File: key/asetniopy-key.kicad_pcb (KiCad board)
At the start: 2 copper layers, 19.1 x 32.6 mm, 4 parts, among them J1 Conn_01x02_Female, SW1 SW_Push

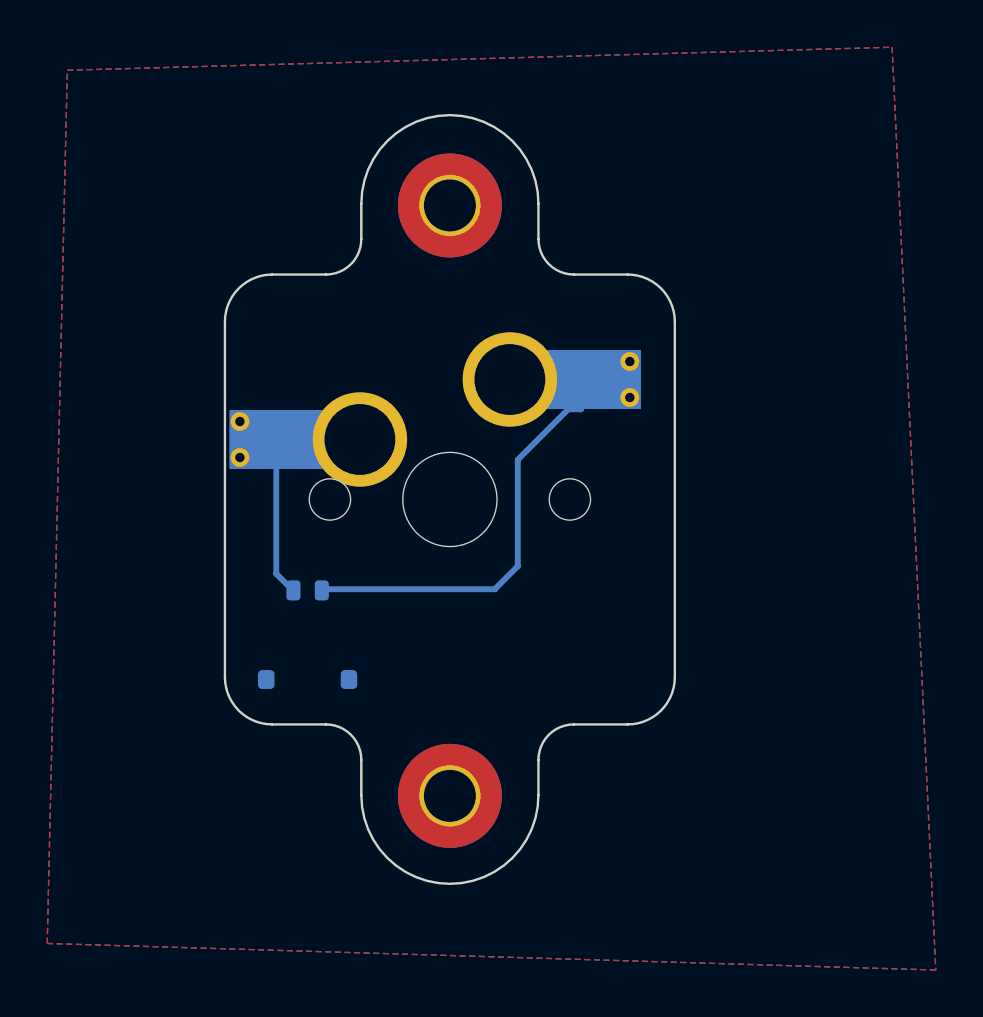
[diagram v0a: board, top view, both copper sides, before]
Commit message: Add mouse bites for key mounting section
* Move keeb.io lib up for re-use of the submodule.
* Add second jumper to the key PCB.
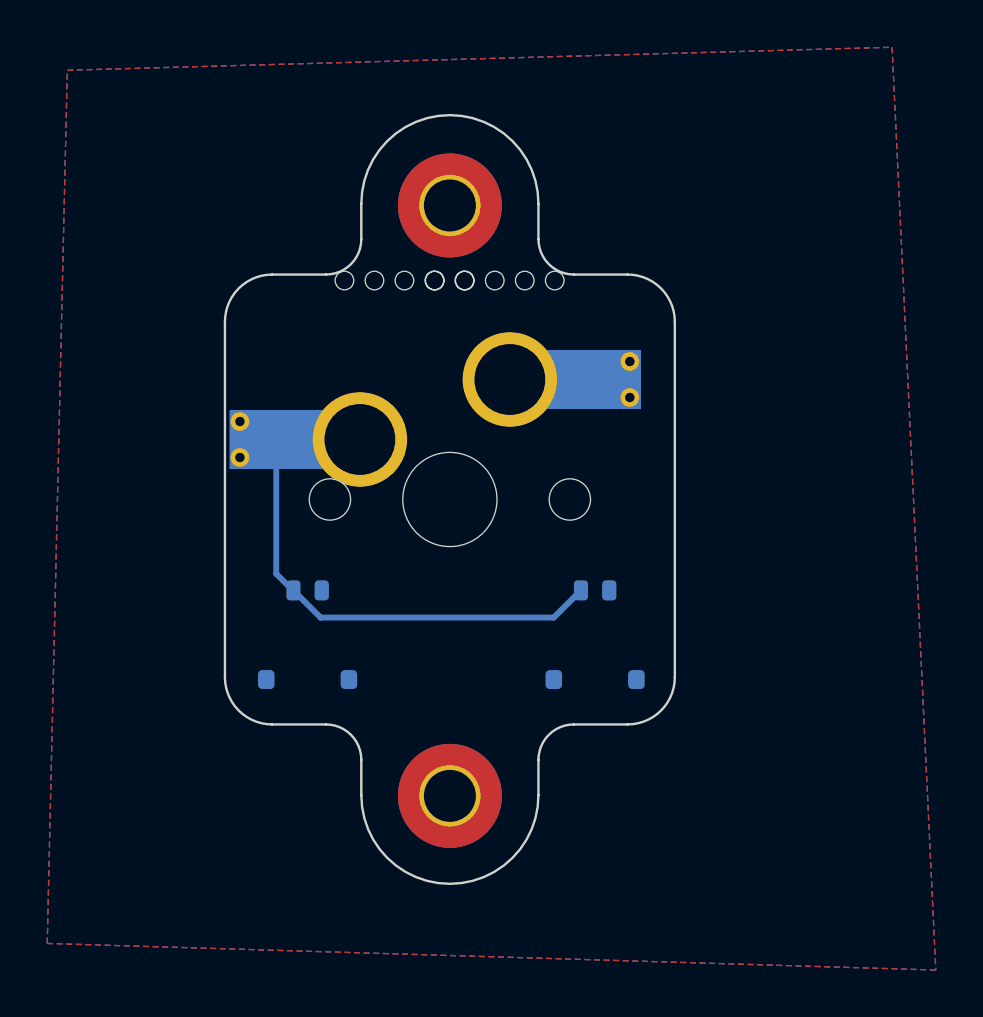
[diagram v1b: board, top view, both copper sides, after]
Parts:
- added J2: Conn_01x02_Female, Connector_Molex:Molex_Pico-EZmate_78171-0002_1x02-1MP_P1.20mm_Vertical, B.Cu at (106.2, 105.7)
- added REF**: breakaway-mousebites, Keebio-Parts:breakaway-mousebites, F.Cu at (101.9, 90.5)
- added REF**: breakaway-mousebites, Keebio-Parts:breakaway-mousebites, F.Cu at (98.1, 90.5)
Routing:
- net Net-(J1-Pad1): track 18.1 -> 0.00 mm
- net Net-(J1-Pad2): track 9.40 -> 22.5 mm
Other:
- board text added: "Use One"
